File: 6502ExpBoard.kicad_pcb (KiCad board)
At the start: 2 copper layers, 90.1 x 52.8 mm, 40 parts, among them J2 Expansion / Diag Port, U1 74LS373, U2 74LS373, U4 74LS373

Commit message: x5
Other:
- board text added: "RETROLOGIC BY TOM SMITH v1 DIAGBOARD"
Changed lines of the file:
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@@
 		(layer "Edge.Cuts")
+	)
+	(gr_text "RETROLOGIC\nBY TOM SMITH v1\nDIAGBOARD"
+		(at 86.973 42.8398 90)
+		(layer "F.SilkS")
+		(effects
+			(font
+				(size 1.5 1.5)
+				(thickness 0.3)
+				(bold yes)
+			)
+			(justify bottom)
+		)
 	)
 	(segment

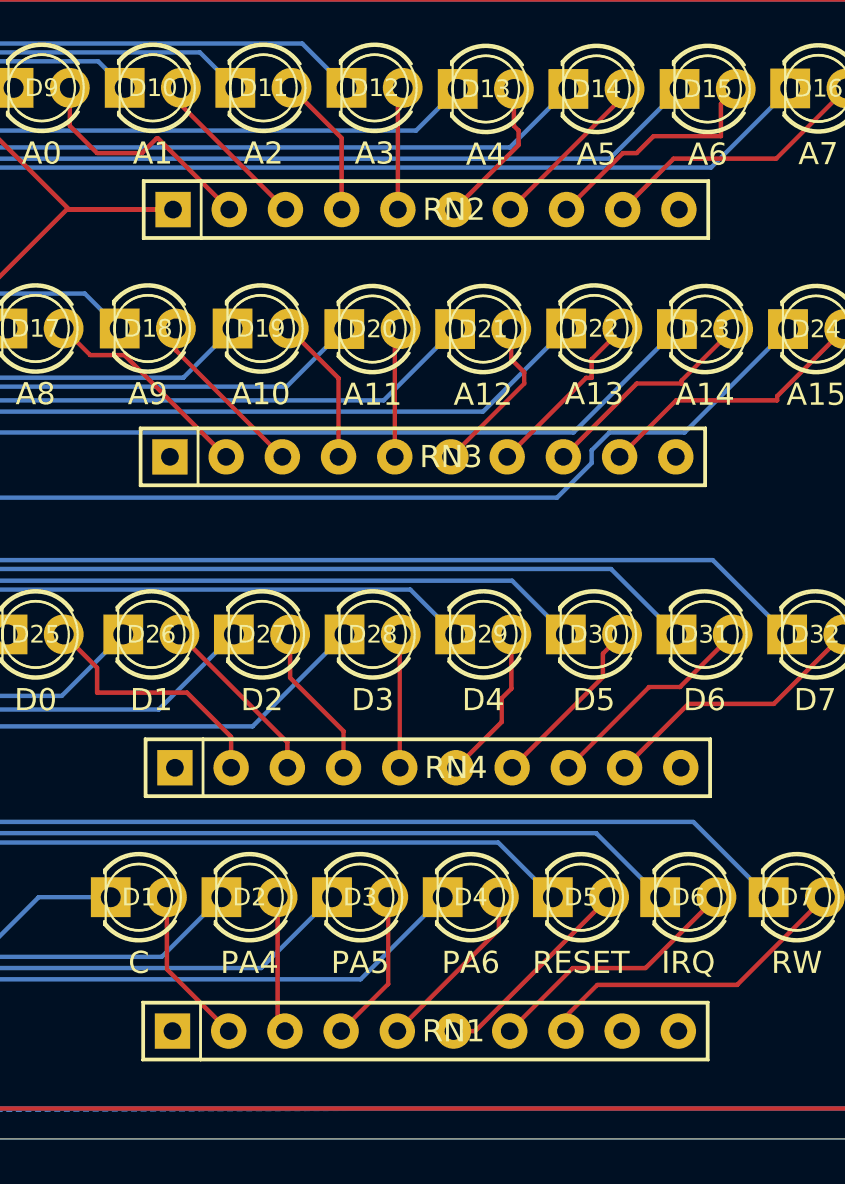
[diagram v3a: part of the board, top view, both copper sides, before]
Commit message: Diag Board led fixes
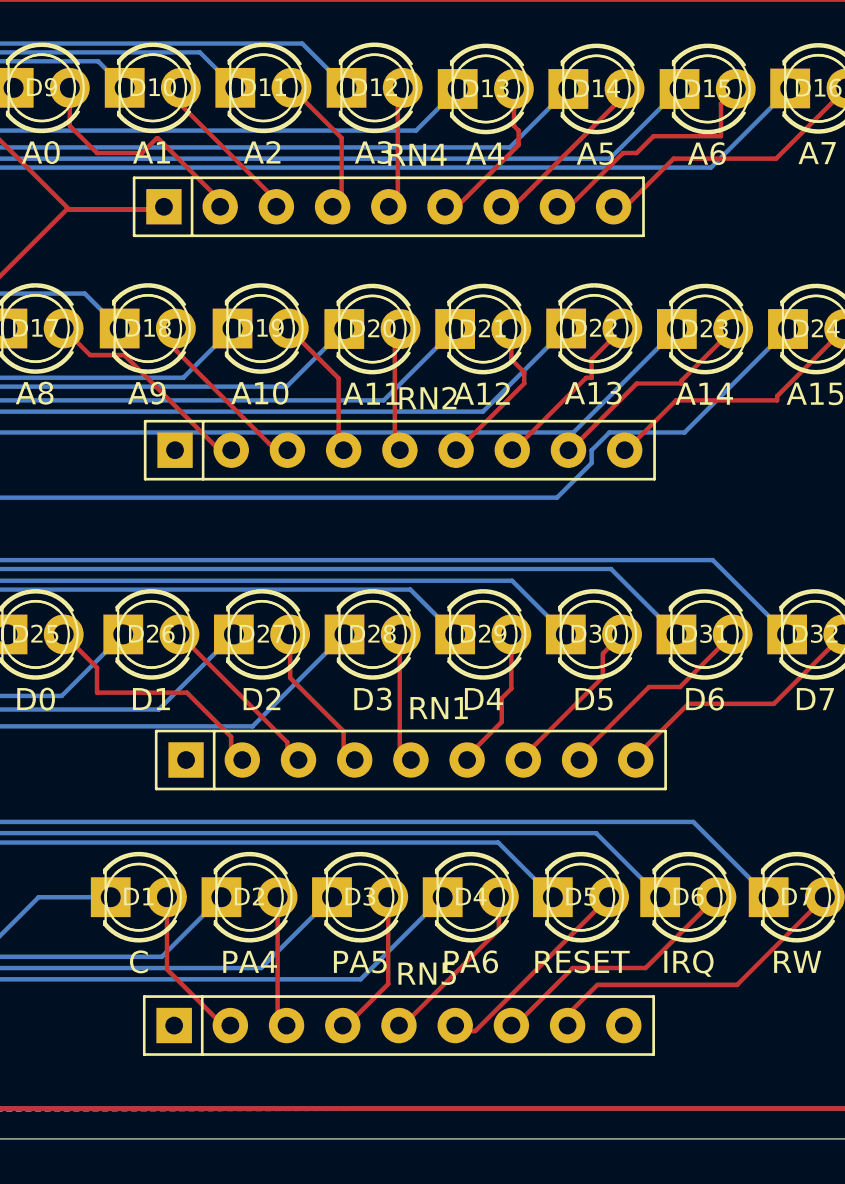
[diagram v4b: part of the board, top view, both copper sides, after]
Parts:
- removed RN3: R_Network09, Resistor_THT:R_Array_SIP10
- added RN5: R_Network08, Resistor_THT:R_Array_SIP9, F.Cu at (124.0, 76.4)
- RN1, RN2, RN4: value R_Network09 -> R_Network08; footprint Resistor_THT:R_Array_SIP10 -> Resistor_THT:R_Array_SIP9
- moved RN4 25.4 mm to (123.5, 39.4)
- moved RN1 12.3 mm to (124.5, 64.4)
- moved RN2 10.9 mm to (124.0, 50.4)
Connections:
- RN1 pad 2: Net-(D1-A) -> Net-(D25-K)
- RN1 pad 3: Net-(D2-A) -> Net-(D26-K)
- RN1 pad 4: Net-(D3-A) -> Net-(D27-K)
- RN1 pad 5: Net-(D4-A) -> Net-(D28-K)
- RN1 pad 6: Net-(D5-A) -> Net-(D29-K)
- RN1 pad 7: Net-(D6-A) -> Net-(D30-K)
- RN1 pad 8: Net-(D7-A) -> Net-(D31-K)
- RN1 pad 9: unconnected-(RN1-R8-Pad9) -> Net-(D32-K)
- RN2 pad 2: Net-(D9-A) -> Net-(D17-K)
- RN2 pad 3: Net-(D10-A) -> Net-(D18-K)
- RN2 pad 4: Net-(D11-A) -> Net-(D19-K)
- RN2 pad 5: Net-(D12-A) -> Net-(D20-K)
- RN2 pad 6: Net-(D13-A) -> Net-(D21-K)
- RN2 pad 7: Net-(D14-A) -> Net-(D22-K)
- RN2 pad 8: Net-(D15-A) -> Net-(D23-K)
- RN2 pad 9: Net-(D16-A) -> Net-(D24-K)
- RN4 pad 2: Net-(D25-A) -> Net-(D9-K)
- RN4 pad 3: Net-(D26-A) -> Net-(D10-K)
- RN4 pad 4: Net-(D27-A) -> Net-(D11-K)
- RN4 pad 5: Net-(D28-A) -> Net-(D12-K)
- RN4 pad 6: Net-(D29-A) -> Net-(D13-K)
- RN4 pad 7: Net-(D30-A) -> Net-(D14-K)
- RN4 pad 8: Net-(D31-A) -> Net-(D15-K)
- RN4 pad 9: Net-(D32-A) -> Net-(D16-K)
- U1 pad 12: Net-(D13-K) -> Net-(D13-A)
- U1 pad 15: Net-(D14-K) -> Net-(D14-A)
- U1 pad 16: Net-(D15-K) -> Net-(D15-A)
- U1 pad 19: Net-(D16-K) -> Net-(D16-A)
- U1 pad 2: Net-(D9-K) -> Net-(D9-A)
- U1 pad 5: Net-(D10-K) -> Net-(D10-A)
- U1 pad 6: Net-(D11-K) -> Net-(D11-A)
- U1 pad 9: Net-(D12-K) -> Net-(D12-A)
- U2 pad 12: Net-(D21-K) -> Net-(D21-A)
- U2 pad 15: Net-(D22-K) -> Net-(D22-A)
- U2 pad 16: Net-(D23-K) -> Net-(D23-A)
- U2 pad 19: Net-(D24-K) -> Net-(D24-A)
- U2 pad 2: Net-(D17-K) -> Net-(D17-A)
- U2 pad 5: Net-(D18-K) -> Net-(D18-A)
- U2 pad 6: Net-(D19-K) -> Net-(D19-A)
- U2 pad 9: Net-(D20-K) -> Net-(D20-A)
- U4 pad 12: Net-(D5-K) -> Net-(D5-A)
- U4 pad 15: Net-(D6-K) -> Net-(D6-A)
- U4 pad 16: Net-(D7-K) -> Net-(D7-A)
- U4 pad 2: Net-(D1-K) -> Net-(D1-A)
- U4 pad 5: Net-(D2-K) -> Net-(D2-A)
- U4 pad 6: Net-(D3-K) -> Net-(D3-A)
- U4 pad 9: Net-(D4-K) -> Net-(D4-A)
- UPackage_DIP:DIP-20_W7.62mm_Socket1 pad 12: Net-(D29-K) -> Net-(D29-A)
- UPackage_DIP:DIP-20_W7.62mm_Socket1 pad 15: Net-(D30-K) -> Net-(D30-A)
- UPackage_DIP:DIP-20_W7.62mm_Socket1 pad 16: Net-(D31-K) -> Net-(D31-A)
- UPackage_DIP:DIP-20_W7.62mm_Socket1 pad 19: Net-(D32-K) -> Net-(D32-A)
- UPackage_DIP:DIP-20_W7.62mm_Socket1 pad 2: Net-(D25-K) -> Net-(D25-A)
- UPackage_DIP:DIP-20_W7.62mm_Socket1 pad 5: Net-(D26-K) -> Net-(D26-A)
- UPackage_DIP:DIP-20_W7.62mm_Socket1 pad 6: Net-(D27-K) -> Net-(D27-A)
- UPackage_DIP:DIP-20_W7.62mm_Socket1 pad 9: Net-(D28-K) -> Net-(D28-A)
